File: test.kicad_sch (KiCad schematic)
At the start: 8 parts, among them U1 AD1853

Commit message: add resistor
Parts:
- added R8: R, symbol Device:R
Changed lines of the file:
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@@
+	(symbol
+		(lib_id "Device:R")
+		(at 156.648 137.938 0)
+		(unit 1)
+		(exclude_from_sim no)
+		(in_bom yes)
+		(on_board yes)
+		(dnp no)
+		(fields_autoplaced yes)
+		(property "Reference" "R8"
+			(at 159.188 136.6679 0)
+			(effects
+				(font
+					(size 1.27 1.27)
+				)
+				(justify left)
+			)
+		)
+		(property "Value" "R"
+			(at 159.188 139.2079 0)
+			(effects
+				(font
+					(size 1.27 1.27)
+				)
+				(justify left)
+			)
+		)
+		(property "Footprint" ""
+			(at 154.87 137.938 90)
+			(effects
+				(font
+					(size 1.27 1.27)
+				)
+				(hide yes)
+			)
+		)
+		(property "Datasheet" "~"
+			(at 156.648 137.938 0)
+			(effects
+				(font
+					(size 1.27 1.27)
+				)
+				(hide yes)
+			)
+		)
+		(property "Description" "Resistor"
+			(at 156.648 137.938 0)
+			(effects
+				(font
+					(size 1.27 1.27)
+				)
+				(hide yes)
+			)
+		)
+		(pin "1"
+		)
+		(pin "2"
+		)
+		(instances
+			(project "test"
+				(path "/836c9f6e-8dd0-464b-ba6e-14d2ae20270a"
+					(reference "R8")
+					(unit 1)
+				)
+			)
+		)
+	)
 	(symbol
 		(lib_id "Device:R")

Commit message: add resistor
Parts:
- added R9: R, symbol Device:R
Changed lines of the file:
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@@
+	(symbol
+		(lib_id "Device:R")
+		(at 160.2881 157.1787 0)
+		(unit 1)
+		(exclude_from_sim no)
+		(in_bom yes)
+		(on_board yes)
+		(dnp no)
+		(fields_autoplaced yes)
+		(property "Reference" "R9"
+			(at 162.8281 155.9086 0)
+			(effects
+				(font
+					(size 1.27 1.27)
+				)
+				(justify left)
+			)
+		)
+		(property "Value" "R"
+			(at 162.8281 158.4486 0)
+			(effects
+				(font
+					(size 1.27 1.27)
+				)
+				(justify left)
+			)
+		)
+		(property "Footprint" ""
+			(at 158.5101 157.1787 90)
+			(effects
+				(font
+					(size 1.27 1.27)
+				)
+				(hide yes)
+			)
+		)
+		(property "Datasheet" "~"
+			(at 160.2881 157.1787 0)
+			(effects
+				(font
+					(size 1.27 1.27)
+				)
+				(hide yes)
+			)
+		)
+		(property "Description" "Resistor"
+			(at 160.2881 157.1787 0)
+			(effects
+				(font
+					(size 1.27 1.27)
+				)
+				(hide yes)
+			)
+		)
+		(pin "1"
+		)
+		(pin "2"
+		)
+		(instances
+			(project "test"
+				(path "/836c9f6e-8dd0-464b-ba6e-14d2ae20270a"
+					(reference "R9")
+					(unit 1)
+				)
+			)
+		)
+	)
 	(symbol
 		(lib_id "Device:R")

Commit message: add resistor
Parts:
- added R10: R, symbol Device:R
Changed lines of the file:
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@@
+	(symbol
+		(lib_id "Device:R")
+		(at 185.769 123.3775 0)
+		(unit 1)
+		(exclude_from_sim no)
+		(in_bom yes)
+		(on_board yes)
+		(dnp no)
+		(fields_autoplaced yes)
+		(property "Reference" "R10"
+			(at 188.309 122.1074 0)
+			(effects
+				(font
+					(size 1.27 1.27)
+				)
+				(justify left)
+			)
+		)
+		(property "Value" "R"
+			(at 188.309 124.6474 0)
+			(effects
+				(font
+					(size 1.27 1.27)
+				)
+				(justify left)
+			)
+		)
+		(property "Footprint" ""
+			(at 183.991 123.3775 90)
+			(effects
+				(font
+					(size 1.27 1.27)
+				)
+				(hide yes)
+			)
+		)
+		(property "Datasheet" "~"
+			(at 185.769 123.3775 0)
+			(effects
+				(font
+					(size 1.27 1.27)
+				)
+				(hide yes)
+			)
+		)
+		(property "Description" "Resistor"
+			(at 185.769 123.3775 0)
+			(effects
+				(font
+					(size 1.27 1.27)
+				)
+				(hide yes)
+			)
+		)
+		(pin "1"
+		)
+		(pin "2"
+		)
+		(instances
+			(project "test"
+				(path "/836c9f6e-8dd0-464b-ba6e-14d2ae20270a"
+					(reference "R10")
+					(unit 1)
+				)
+			)
+		)
+	)
 	(symbol
 		(lib_id "Device:R")

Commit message: add resistor
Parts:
- added R11: R, symbol Device:R
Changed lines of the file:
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@@
+	(symbol
+		(lib_id "Device:R")
+		(at 205.0097 130.3111 0)
+		(unit 1)
+		(exclude_from_sim no)
+		(in_bom yes)
+		(on_board yes)
+		(dnp no)
+		(fields_autoplaced yes)
+		(property "Reference" "R11"
+			(at 207.5497 129.041 0)
+			(effects
+				(font
+					(size 1.27 1.27)
+				)
+				(justify left)
+			)
+		)
+		(property "Value" "R"
+			(at 207.5497 131.581 0)
+			(effects
+				(font
+					(size 1.27 1.27)
+				)
+				(justify left)
+			)
+		)
+		(property "Footprint" ""
+			(at 203.2317 130.3111 90)
+			(effects
+				(font
+					(size 1.27 1.27)
+				)
+				(hide yes)
+			)
+		)
+		(property "Datasheet" "~"
+			(at 205.0097 130.3111 0)
+			(effects
+				(font
+					(size 1.27 1.27)
+				)
+				(hide yes)
+			)
+		)
+		(property "Description" "Resistor"
+			(at 205.0097 130.3111 0)
+			(effects
+				(font
+					(size 1.27 1.27)
+				)
+				(hide yes)
+			)
+		)
+		(pin "1"
+		)
+		(pin "2"
+		)
+		(instances
+			(project "test"
+				(path "/836c9f6e-8dd0-464b-ba6e-14d2ae20270a"
+					(reference "R11")
+					(unit 1)
+				)
+			)
+		)
+	)
 	(symbol
 		(lib_id "Device:R")

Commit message: add resistor
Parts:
- added R12: R, symbol Device:R
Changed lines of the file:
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@@
+	(symbol
+		(lib_id "Device:R")
+		(at 218.1834 128.231 0)
+		(unit 1)
+		(exclude_from_sim no)
+		(in_bom yes)
+		(on_board yes)
+		(dnp no)
+		(fields_autoplaced yes)
+		(property "Reference" "R12"
+			(at 220.7234 126.9609 0)
+			(effects
+				(font
+					(size 1.27 1.27)
+				)
+				(justify left)
+			)
+		)
+		(property "Value" "R"
+			(at 220.7234 129.5009 0)
+			(effects
+				(font
+					(size 1.27 1.27)
+				)
+				(justify left)
+			)
+		)
+		(property "Footprint" ""
+			(at 216.4054 128.231 90)
+			(effects
+				(font
+					(size 1.27 1.27)
+				)
+				(hide yes)
+			)
+		)
+		(property "Datasheet" "~"
+			(at 218.1834 128.231 0)
+			(effects
+				(font
+					(size 1.27 1.27)
+				)
+				(hide yes)
+			)
+		)
+		(property "Description" "Resistor"
+			(at 218.1834 128.231 0)
+			(effects
+				(font
+					(size 1.27 1.27)
+				)
+				(hide yes)
+			)
+		)
+		(pin "1"
+		)
+		(pin "2"
+		)
+		(instances
+			(project "test"
+				(path "/836c9f6e-8dd0-464b-ba6e-14d2ae20270a"
+					(reference "R12")
+					(unit 1)
+				)
+			)
+		)
+	)
 	(symbol
 		(lib_id "Device:R")

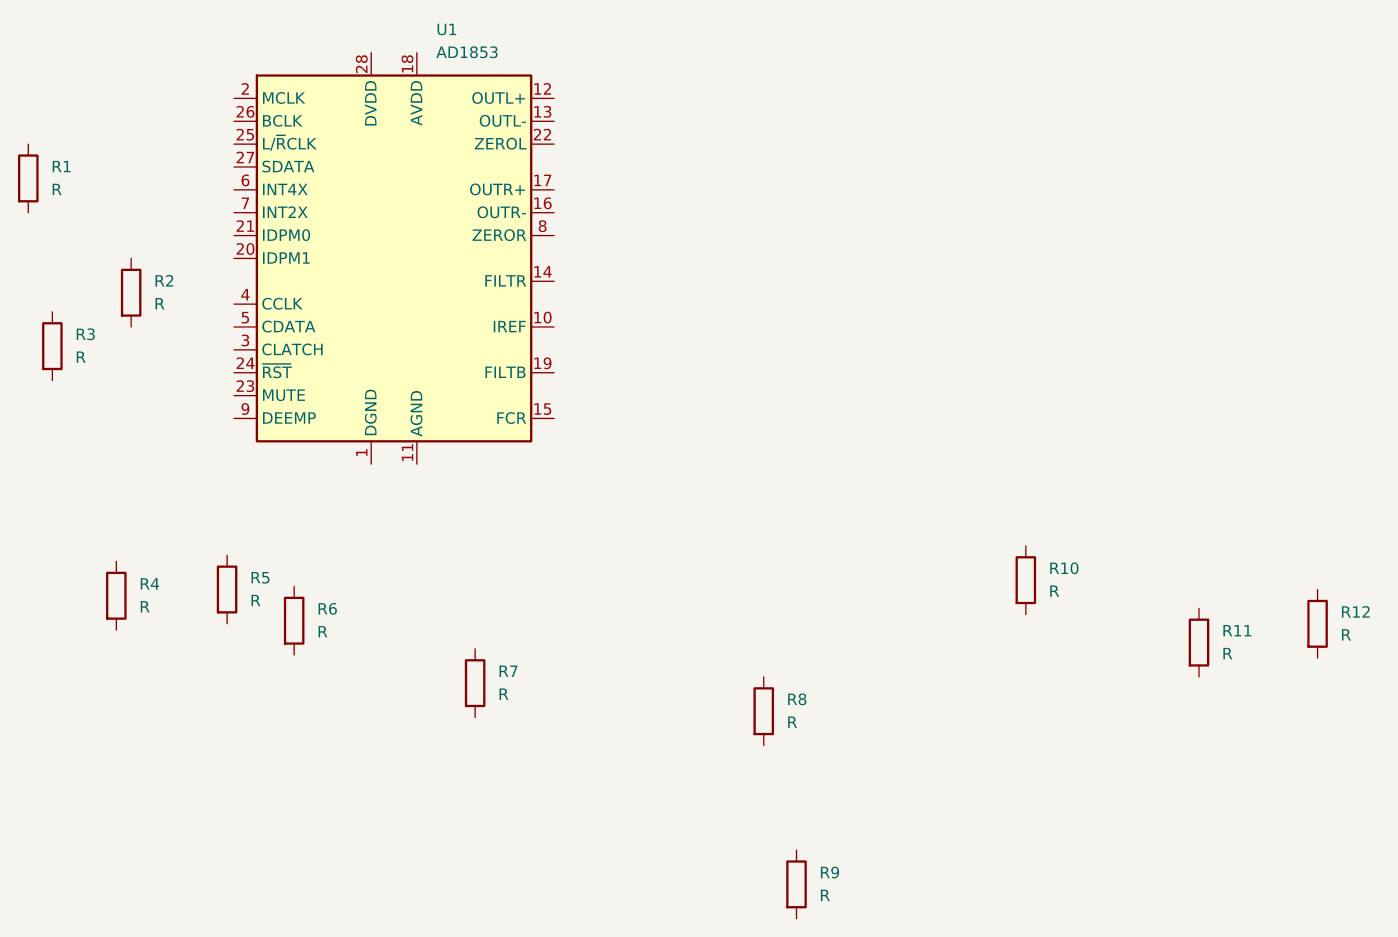
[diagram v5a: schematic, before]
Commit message: new connection system
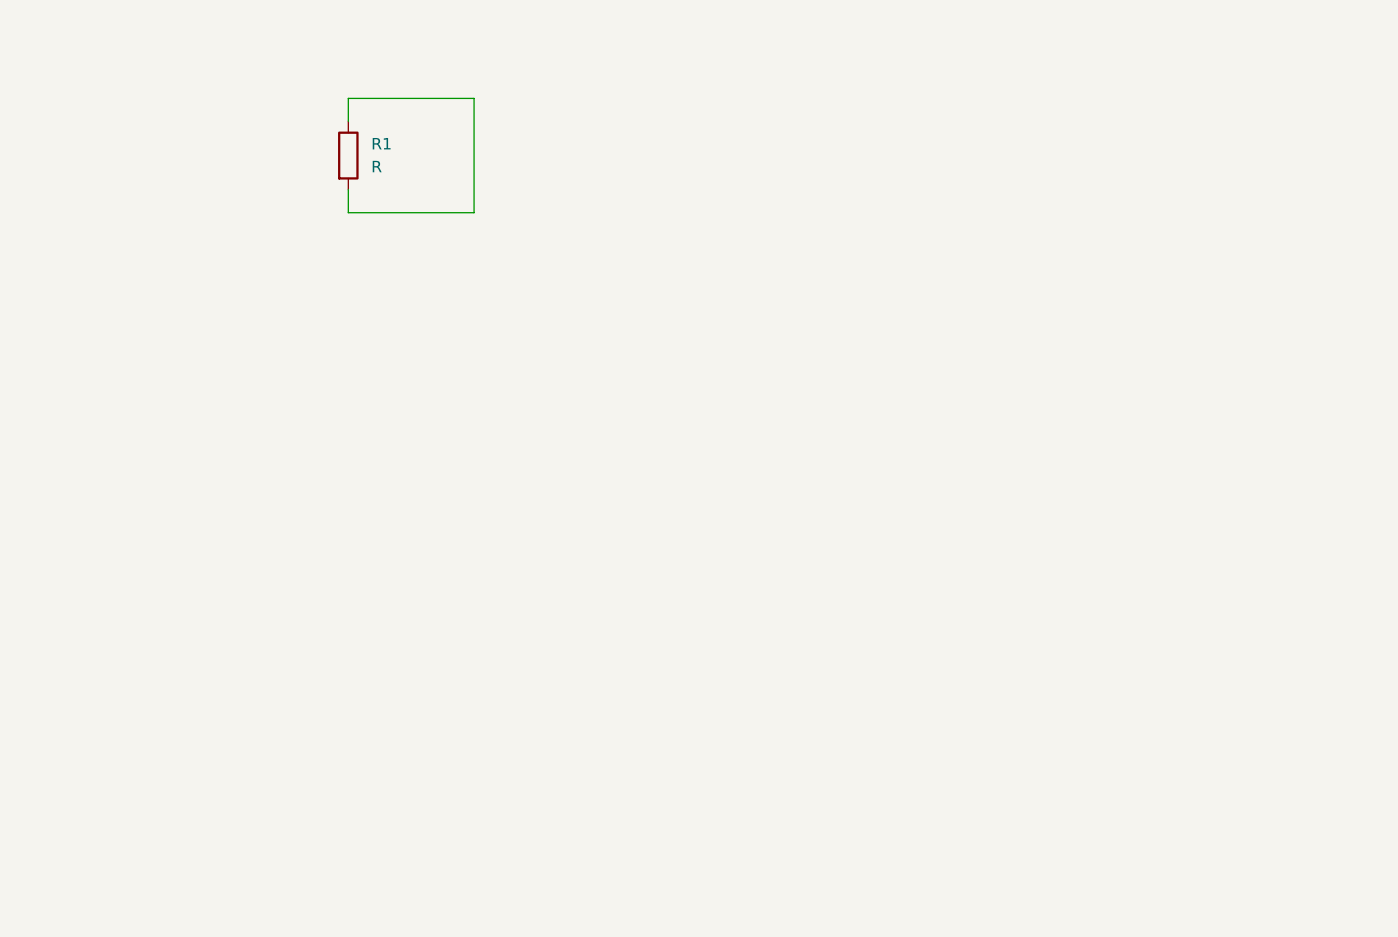
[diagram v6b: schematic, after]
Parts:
- removed R10, R11, R12, R2, R3, R4, R5, R6, R7, R8, R9: R, symbol Device:R
- removed U1: AD1853, Package_SO:SSOP-28_5.3x10.2mm_P0.65mm, symbol Audio:AD1853
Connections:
- net at R1.1: now also R1.2

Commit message: add resistor
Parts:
- added R2: R, symbol Device:R
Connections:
- net at R1.1: now also R2.1; no longer R1.2
- new net: R1.2, R2.2
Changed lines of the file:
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@@
+	(wire
+		(pts
+			(xy 124.46 80.01) (xy 124.46 82.55)
+		)
+		(stroke
+			(width 0)
+			(type default)
+		)
+	)
 	(wire
 		(pts
@@
 	(wire
 		(pts
-			(xy 124.46 69.85) (xy 124.46 82.55)
+			(xy 124.46 69.85) (xy 124.46 72.39)
 		)
 		(stroke
@@
 					(unit 1)
 				)
+			)
+		)
+	)
+	(symbol
+		(lib_id "Device:R")
+		(at 124.46 76.2 0)
+		(unit 1)
+		(exclude_from_sim no)
+		(in_bom yes)
+		(on_board yes)
+		(dnp no)
+		(fields_autoplaced yes)
+		(property "Reference" "R2"
+			(at 127 74.9299 0)
+			(effects
+				(font
+					(size 1.27 1.27)
+				)
+				(justify left)
+			)
+		)
+		(property "Value" "R"
+			(at 127 77.4699 0)
+			(effects
+				(font
+					(size 1.27 1.27)
+				)
+				(justify left)
+			)
+		)
+		(property "Footprint" ""
+			(at 122.682 76.2 90)
+			(effects
+				(font
+					(size 1.27 1.27)
+				)
+				(hide yes)
+			)
+		)
+		(property "Datasheet" "~"
+			(at 124.46 76.2 0)
+			(effects
+				(font
+					(size 1.27 1.27)
+				)
+				(hide yes)
+			)
+		)
+		(property "Description" "Resistor"
+			(at 124.46 76.2 0)
+			(effects
+				(font
+					(size 1.27 1.27)
+				)
+				(hide yes)
+			)
+		)
+		(pin "1"
+		)
+		(pin "2"
+		)
+		(instances
+			(project "test"
+				(path "/836c9f6e-8dd0-464b-ba6e-14d2ae20270a"
+					(reference "R2")
+					(unit 1)
+				)

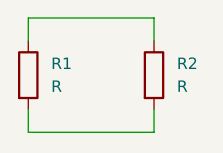
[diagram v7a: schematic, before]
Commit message: added net label
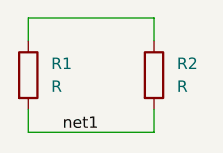
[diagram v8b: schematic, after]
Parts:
- R1, R2: footprint (none) -> Resistor_SMD:R_1210_3225Metric_Pad1.30x2.65mm_HandSolder
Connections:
- net net1: now reaches R1.2, R2.2
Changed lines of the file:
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@@
+		)
+	)
+	(label "net1"
+		(at 114.3 82.55 0)
+		(effects
+			(font
+				(size 1.27 1.27)
+			)
+			(justify left bottom)
 		)
 	)
@@
 			)
 		)
-		(property "Footprint" ""
+		(property "Footprint" "Resistor_SMD:R_1210_3225Metric_Pad1.30x2.65mm_HandSolder"
 			(at 108.712 76.2 90)
 			(effects
@@
 			)
 		)
-		(property "Footprint" ""
+		(property "Footprint" "Resistor_SMD:R_1210_3225Metric_Pad1.30x2.65mm_HandSolder"
 			(at 122.682 76.2 90)
 			(effects
